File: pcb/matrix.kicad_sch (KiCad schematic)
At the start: 242 parts, among them SW1 Rotary_Encoder_Switch

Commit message: cleanup project
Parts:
- SW1: symbol basketweave-rescue:Rotary_Encoder_Switch-Device -> keeb-comps:Rotary_Encoder_Switch
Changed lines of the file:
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@@
 	)
 	(symbol
-		(lib_id "basketweave-rescue:Rotary_Encoder_Switch-Device")
+		(lib_id "keeb-comps:Rotary_Encoder_Switch")
 		(at 306.07 204.47 180)
 		(unit 1)

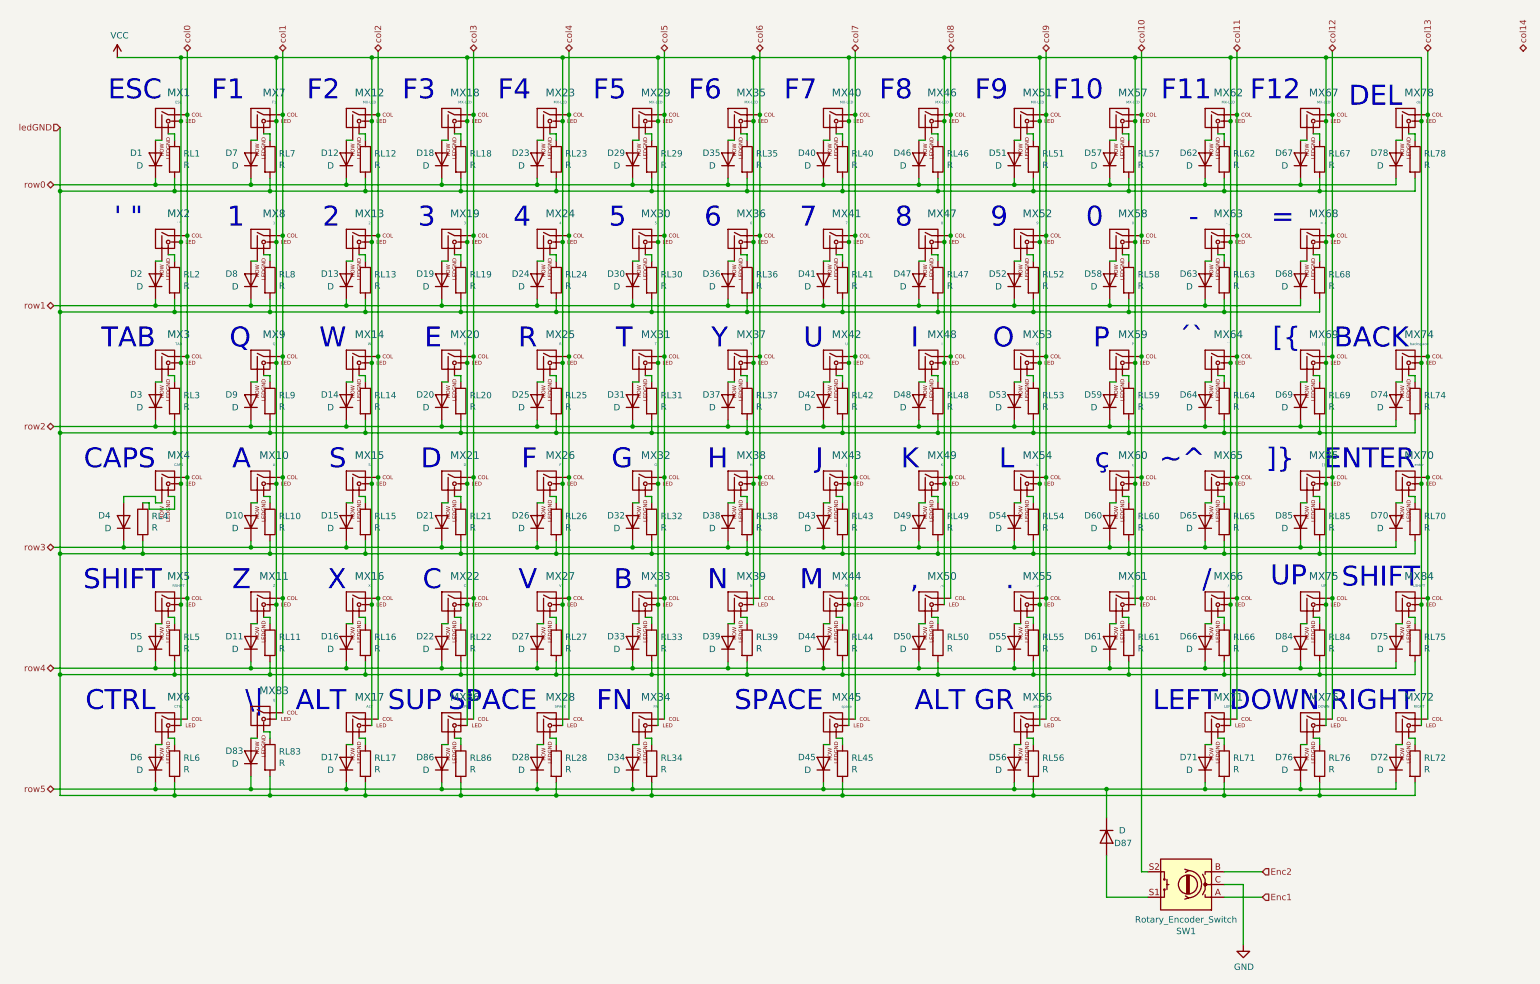
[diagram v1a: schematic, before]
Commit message: changes key footprints to hotswap + SMD LEDs
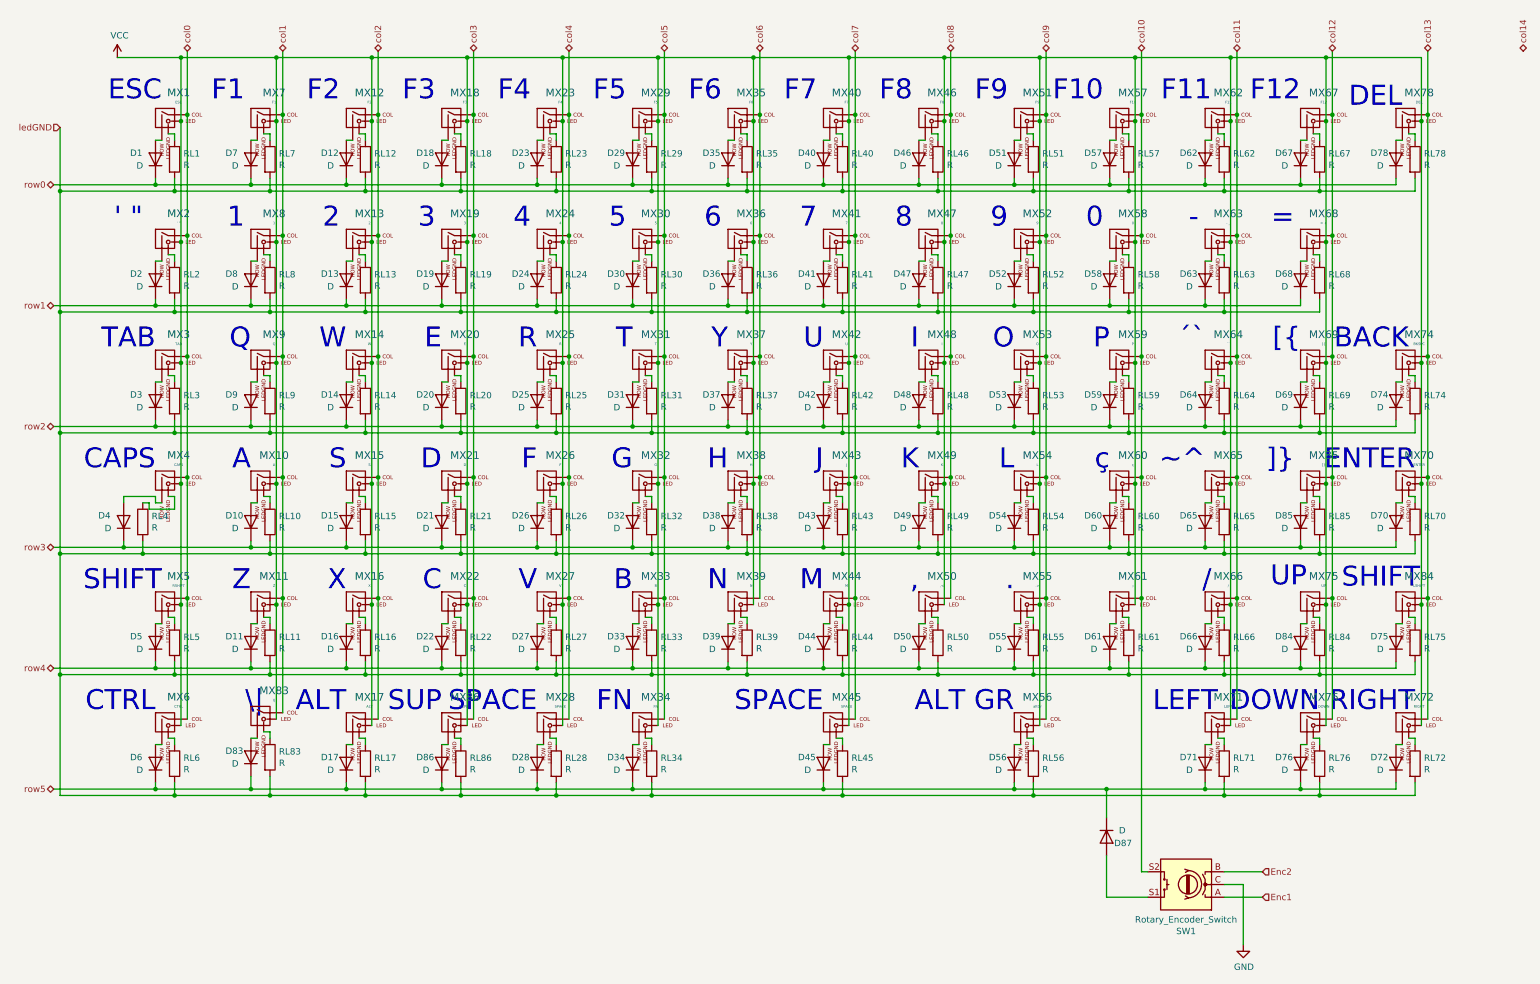
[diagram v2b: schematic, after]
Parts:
- MX1, MX10, MX11, MX13, MX14, MX15, MX16, MX19, MX2, MX20, MX21, MX22, MX24, MX25, MX26, MX27, MX30, MX31, MX32, MX33, MX34, MX36, MX37, MX38, MX39, MX41, MX42, MX43, MX44, MX47, MX48, MX49, MX50, MX52, MX53, MX54, MX55, MX58, MX59, MX60, MX61, MX63, MX64, MX65, MX66, MX68, MX69, MX7, MX71, MX72, MX75, MX76, MX8, MX83, MX84, MX85, MX9: footprint ai03-MX_only:MXOnly-1U -> ai03-MX_only:MXOnly-1U-Hotswap-Antishear-Led-SMD
- MX12: value MX-LED -> F2; footprint ai03-MX_only:MXOnly-1U -> ai03-MX_only:MXOnly-1U-Hotswap-Antishear-Led-SMD
- MX17, MX3, MX56, MX6, MX86: footprint ai03-MX_only:MXOnly-1.5U -> ai03-MX_only:MXOnly-1.5U-Hotswap-Antishear-Led-SMD
- MX18: value MX-LED -> F3; footprint ai03-MX_only:MXOnly-1U -> ai03-MX_only:MXOnly-1U-Hotswap-Antishear-Led-SMD
- MX23: value MX-LED -> F4; footprint ai03-MX_only:MXOnly-1U -> ai03-MX_only:MXOnly-1U-Hotswap-Antishear-Led-SMD
- MX28: footprint ai03-MX_only:MXOnly-2U-ReversedStabilizers -> ai03-MX_only:MXOnly-2U-RevStab-Hotswap-Antishear-Led-SMD
- MX29: value MX-LED -> F5; footprint ai03-MX_only:MXOnly-1U -> ai03-MX_only:MXOnly-1U-Hotswap-Antishear-Led-SMD
- MX35: value MX-LED -> F6; footprint ai03-MX_only:MXOnly-1U -> ai03-MX_only:MXOnly-1U-Hotswap-Antishear-Led-SMD
- MX4: footprint ai03-MX_only:MXOnly-1.75U -> ai03-MX_only:MXOnly-1.75U-Hotswap-Antishear-Led-SMD
- MX40: value MX-LED -> F7; footprint ai03-MX_only:MXOnly-1U -> ai03-MX_only:MXOnly-1U-Hotswap-Antishear-Led-SMD
- MX45: value space -> SPACE; footprint ai03-MX_only:MXOnly-2.75U-ReversedStabilizers -> ai03-MX_only:MXOnly-2.75U-RevStab-Hotswap-Antishear-Led-SMD
- MX46: value MX-LED -> F8; footprint ai03-MX_only:MXOnly-1U -> ai03-MX_only:MXOnly-1U-Hotswap-Antishear-Led-SMD
- MX5: footprint ai03-MX_only:MXOnly-1.25U -> ai03-MX_only:MXOnly-1.25U-Hotswap-Antishear-Led-SMD
- MX51: value MX-LED -> F9; footprint ai03-MX_only:MXOnly-1U -> ai03-MX_only:MXOnly-1U-Hotswap-Antishear-Led-SMD
- MX57: value MX-LED -> F10; footprint ai03-MX_only:MXOnly-1U -> ai03-MX_only:MXOnly-1U-Hotswap-Antishear-Led-SMD
- MX62: value MX-LED -> F11; footprint ai03-MX_only:MXOnly-1U -> ai03-MX_only:MXOnly-1U-Hotswap-Antishear-Led-SMD
- MX67: value MX-LED -> F12; footprint ai03-MX_only:MXOnly-1U -> ai03-MX_only:MXOnly-1U-Hotswap-Antishear-Led-SMD
- MX70: value enter -> ENTER; footprint ai03-MX_only:MXOnly-ISO -> ai03-MX_only:MXOnly-ISO-Hotswap-Antishear-Led-SMD
- MX74: value backspace -> BKSPC; footprint ai03-MX_only:MXOnly-2U -> ai03-MX_only:MXOnly-2U-Hotswap-Antishear-Led-SMD
- MX78: value del -> DEL; footprint ai03-MX_only:MXOnly-1U -> ai03-MX_only:MXOnly-1U-Hotswap-Antishear-Led-SMD
